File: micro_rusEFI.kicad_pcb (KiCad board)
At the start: 2 copper layers, 80.6 x 93.7 mm, 254 parts, among them J1 USB_B_Mini, J12 Conn_01x01, J13 Conn_01x01, J15 Conn_01x01, J17 Conn_01x01, J19 Conn_01x06, J2 Conn_02x05_Odd_Even, J3 Conn_01x01, J4 Conn_02x05_Counter_Clockwise, J5 Conn_01x01, J6 Micro_SD_Card_Det, J7 TC2030, Q1 IPD30N06S2L-23, SW1 SW_Push, SW2 SW_Push, SW3 SW_Push, SW4 SW_Push, U1 STM32F427VGT6, U10 VNLD5090, U2 TLE8888QK, U3 molex_48pin_MRE, U31 MIC4427, U32 MIC4427, U33 MIC4427, U35 MCP6004, U36 MCP6004, U4 TLE9201SG, U46 MCP6004, U5 LM1117-3.3, U7 XC6206 3.3V, U8 MCP6004, U9 VNLD5090, X1 8MHz 20pF, Y2 32768 Hz

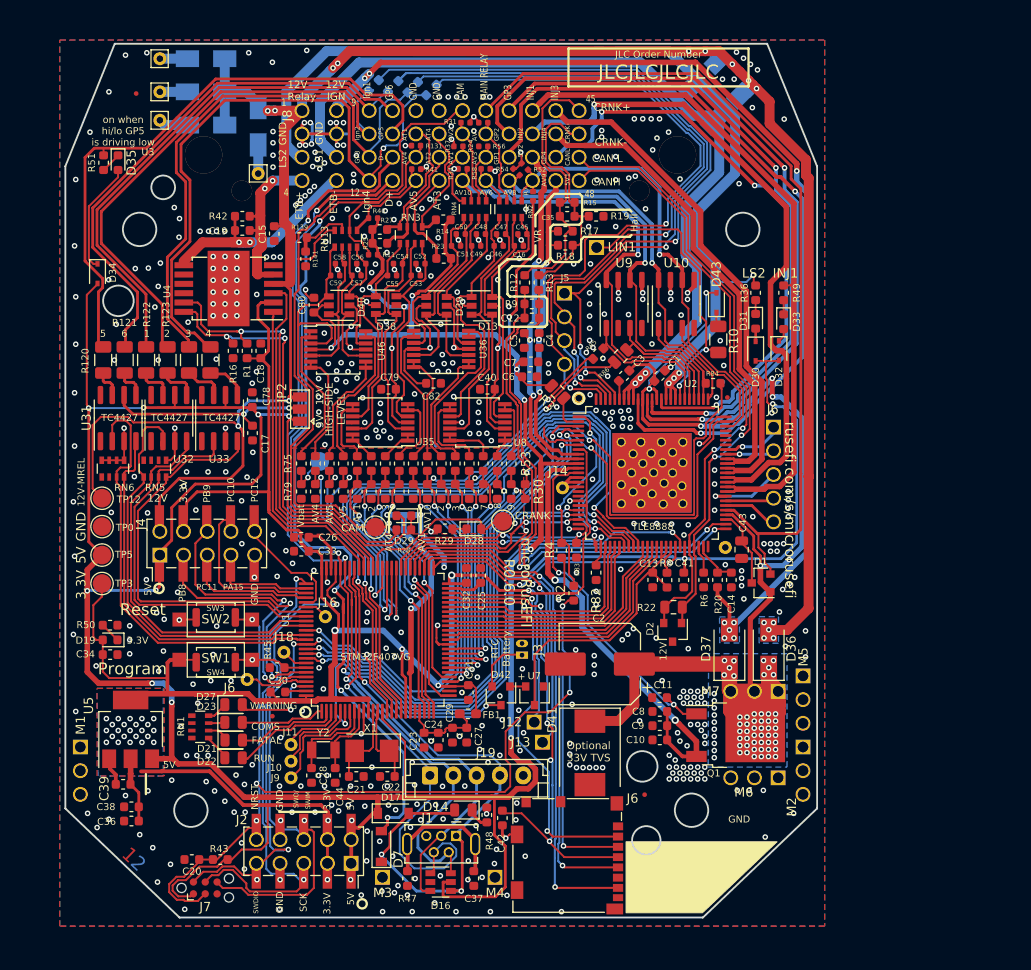
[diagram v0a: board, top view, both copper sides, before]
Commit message: replaces micro b connector by usb-c
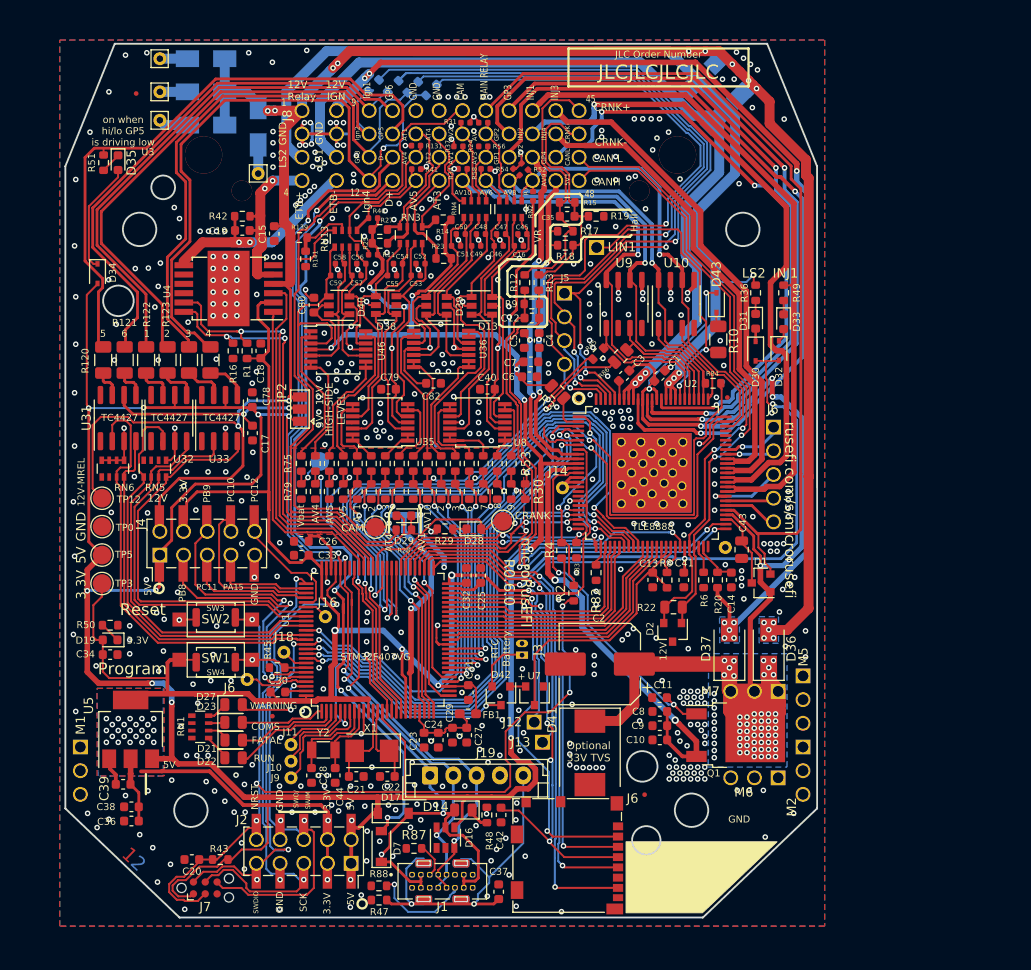
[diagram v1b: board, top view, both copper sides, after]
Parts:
- added R87: 5.1k, Resistor_SMD:R_0603_1608Metric, F.Cu at (58.0, 108.7)
- added R88: 5.1k, Resistor_SMD:R_0603_1608Metric, F.Cu at (54.2, 112.7)
- J1: value USB_B_Mini -> UJ20-C-V-C-2-SMT-TR; footprint hellen-one-common:USB-MINI-B-VERTICAL -> UJ20_C_V_C_2_SMT_TR:CUI_UJ20-C-V-C-2-SMT-TR
- moved D16 4.79 mm to (61.4, 107.5), turned to 90 degrees
- moved J1 3.98 mm to (61.0, 112.2), turned to 0 degrees
- moved R47 3.83 mm to (54.2, 114.2), turned to 180 degrees
- moved C37 3.02 mm to (67.1, 113.3), turned to 90 degrees
- moved C33 0.43 mm to (45.9, 77.2)
- moved C26 0.43 mm to (45.9, 75.7)
- moved C42 0.35 mm to (67.3, 105.1)
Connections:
- D14 pad 2: /MCU/PA9 -> /MCU/Vbus
- D16 pad 1: /MCU/PA10 -> unconnected-(D16-Pad1)
- D16 pad 4: /MCU/PA9 -> /5V
- D16 pad 5: /5V -> /MCU/Vbus
- D17 pad 2: /MCU/PA9 -> /MCU/Vbus
- D7 pad 1: /MCU/PA9 -> /MCU/Vbus
- J19 pad 1: /MCU/PA10 -> /MCU/Vbus
- J19 pad 4: /MCU/PA9 -> GND
- J19 pad 5: GND -> /MCU/shield
- NT1 pad 1: Net-(NT1-Pad1) -> /MCU/PA9
- NT1 pad 2: /MCU/PA9 -> /MCU/Vbus
- U1 pad 68: Net-(NT1-Pad1) -> /MCU/PA9
- U1 pad 69: /MCU/PA10 -> unconnected-(U1-PA10-Pad69)
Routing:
- net /MCU/PA9: track 67.2 -> 2.66 mm, vias 3 -> 0
- net /MCU/Vbus: track 0.00 -> 59.8 mm, vias 0 -> 3
- net /MCU/PA10: track 49.8 -> 0.00 mm, vias 1 -> 0
- net /MCU/shield: track 15.2 -> 41.2 mm, vias 0 -> 2
- net /5V: track 465.8 -> 450.3 mm
- net Net-(J1-CC2): track 0.00 -> 10.7 mm, vias 0 -> 1
- net Net-(J1-CC1): track 0.00 -> 3.74 mm
- net GND: track 111.8 -> 108.7 mm, vias 525 -> 511
- net Net-(NT1-Pad1): track 2.66 -> 0.00 mm
- net /USB_D+: track 100.1 -> 98.4 mm, vias 3 -> 4
- net /VDD: track 308.8 -> 307.5 mm
- net /USB_D-: track 101.6 -> 100.5 mm, vias 3 -> 4
- net /H-BRIDGE/DIR: track 33.7 -> 34.3 mm
- net /H-BRIDGE/SO: track 37.5 -> 38.1 mm

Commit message: Impedence controlled USB traces
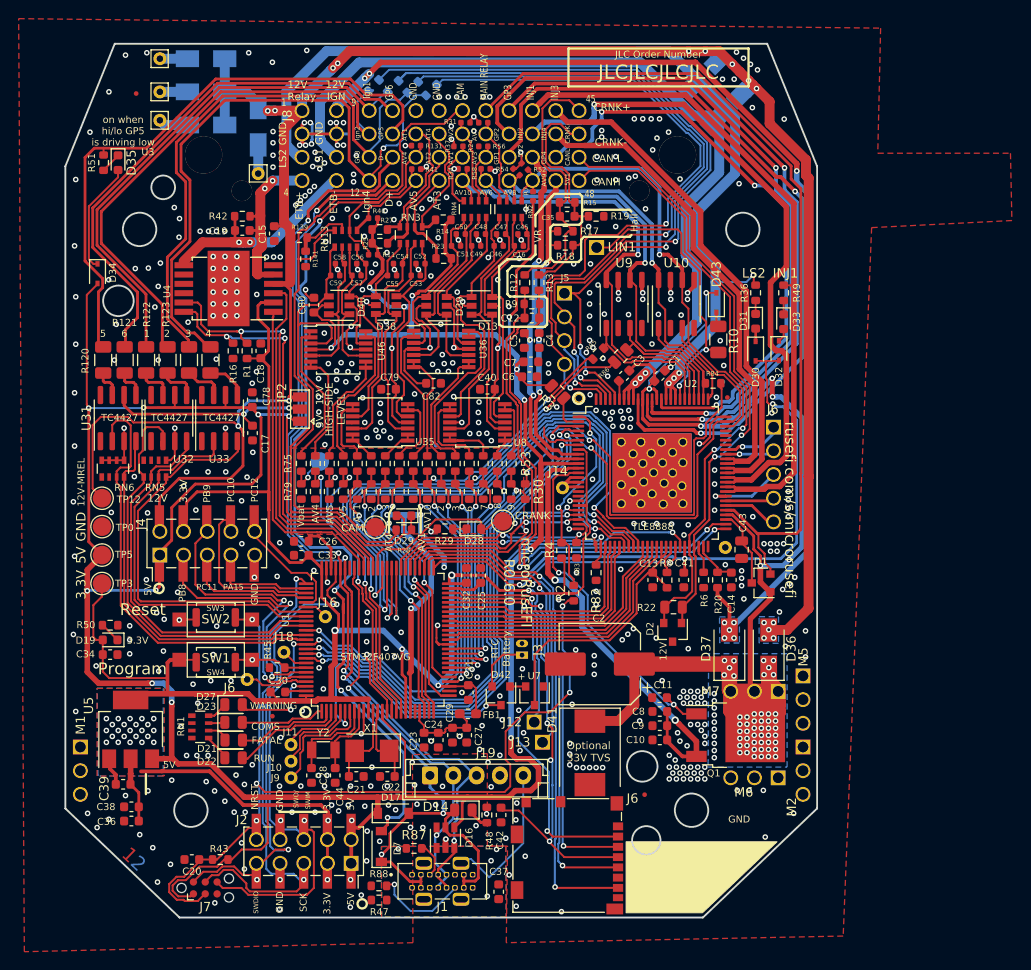
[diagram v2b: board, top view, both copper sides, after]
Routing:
- net /MCU/shield: track 41.2 -> 16.3 mm, vias 2 -> 0
- net GND: track 108.7 -> 109.7 mm, vias 511 -> 512
- net /5V: track 450.3 -> 451.1 mm
- net Net-(J1-CC2): track 10.7 -> 10.2 mm
- added copper zone on B.Cu, net /MCU/shield
- added copper zone on F.Cu, net /MCU/shield
- added copper zone on In1.Cu, net GND
- added copper zone on In2.Cu, net GND
- removed copper zone on B.Cu, net GND
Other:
- copper layers 2 -> 4

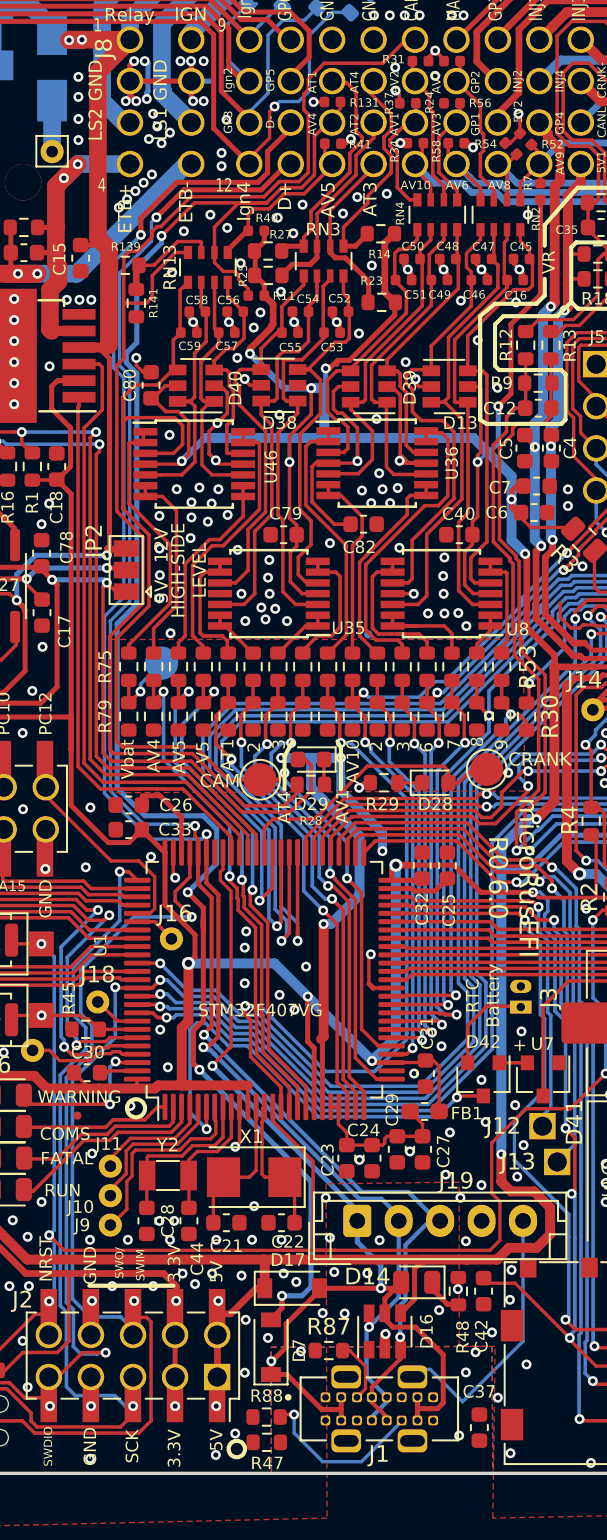
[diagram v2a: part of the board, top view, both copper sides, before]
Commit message: widened usb trace to further reduce impedence
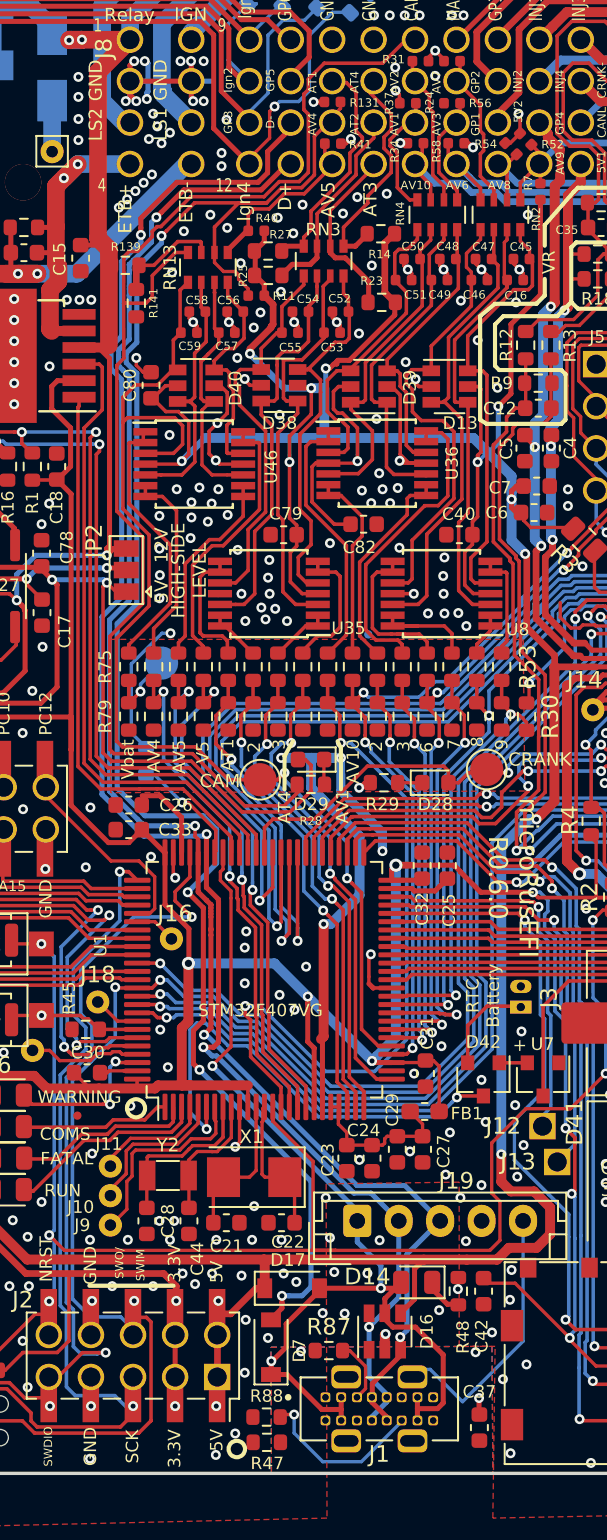
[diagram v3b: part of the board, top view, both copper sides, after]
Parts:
- added R89: 10K, Resistor_SMD:R_0603_1608Metric, B.Cu at (46.9, 73.1)
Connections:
- U1 pad 69: unconnected-(U1-PA10-Pad69) -> Net-(U1-PA10)
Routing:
- net GND: track 109.7 -> 119.2 mm, vias 512 -> 511
- net Net-(U1-PA10): track 0.00 -> 6.97 mm, vias 0 -> 1
- net /AV4: track 104.3 -> 102.2 mm
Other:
- board text added: "PA10 PULL-DOWN"
